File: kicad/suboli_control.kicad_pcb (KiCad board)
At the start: 2 copper layers, 125 x 95 mm, 45 parts, among them J1 DC barrel jack panel header 5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, J2 3.5 mm TRS input panel header, J4 3.5 mm TRS headphone panel he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, J5 MA12070 module power, J6 MA12070 module audio in, SW1 DPST power switch panel header, U1 TLE2426ILP

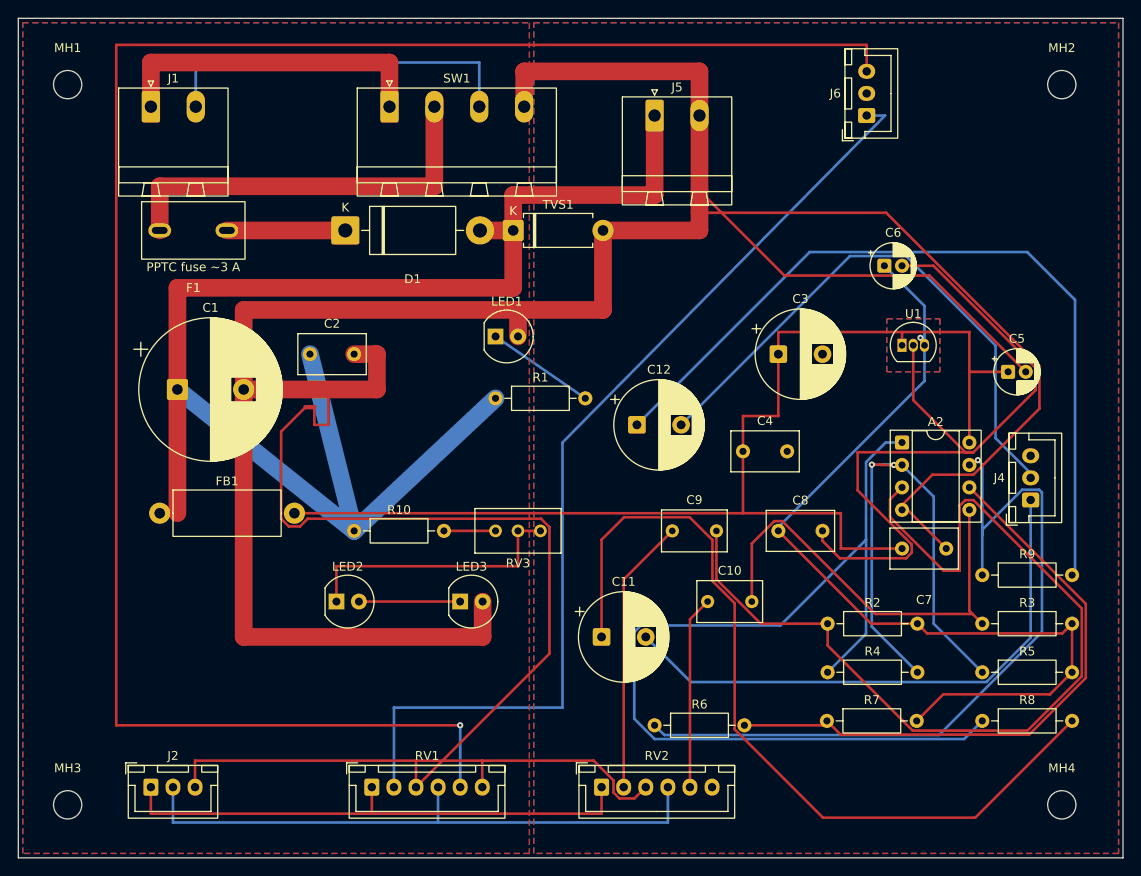
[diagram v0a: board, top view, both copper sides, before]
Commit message: R14: ground stitching vias
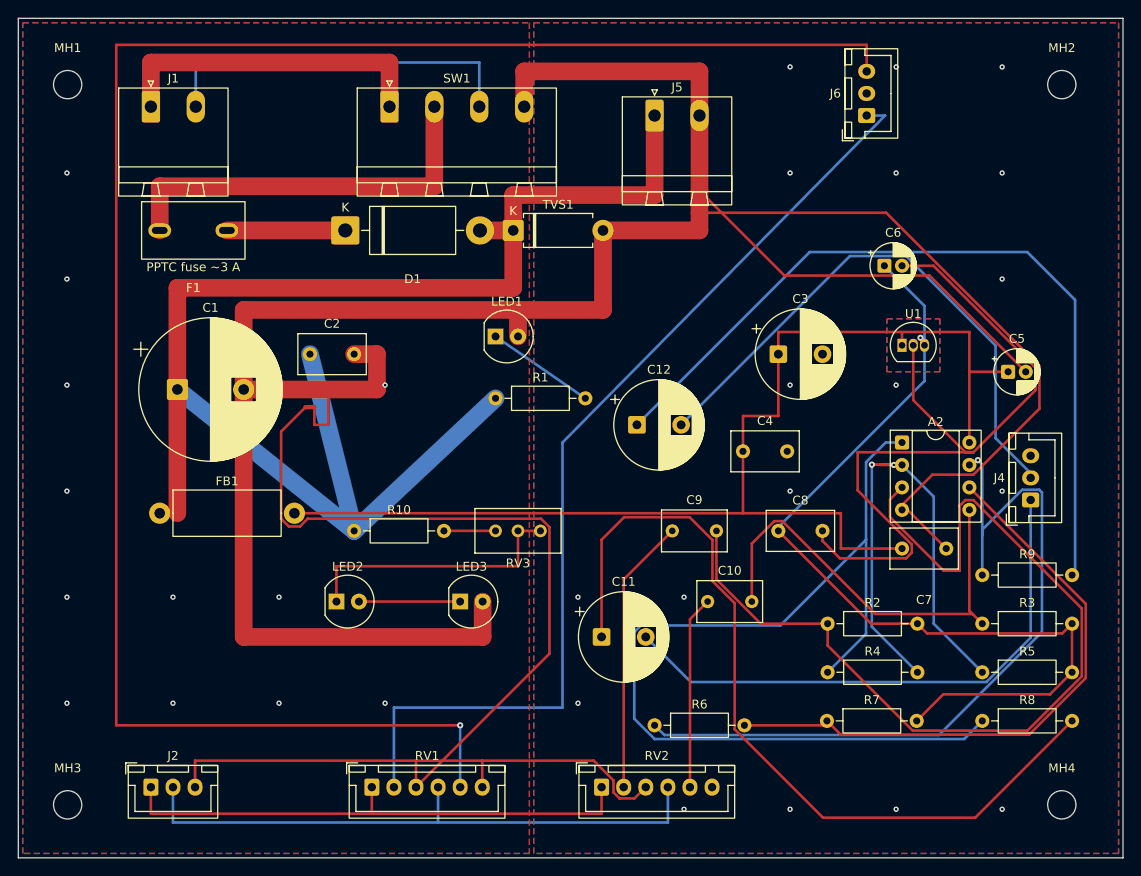
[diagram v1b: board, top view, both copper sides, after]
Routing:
- net /GND_STAR: vias 0 -> 13
- net /GND_SIG: vias 0 -> 18
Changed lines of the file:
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@@
 		(capping no)
 		(filling no)
-		(zone_defaults)
 		(aux_axis_origin 11.92 107)
 		(pcbplotparams
@@
 		(net "/GND_STAR")
 	)
+	(via
+		(at 29.42 77.5)
+		(size 0.6)
+		(drill 0.3)
+		(layers "F.Cu" "B.Cu")
+		(net "/GND_STAR")
+	)
+	(via
+		(at 41.42 53.5)
+		(size 0.6)
+		(drill 0.3)
+		(layers "F.Cu" "B.Cu")
+		(net "/GND_STAR")
+	)
+	(via
+		(at 17.42 65.5)
+		(size 0.6)
+		(drill 0.3)
+		(layers "F.Cu" "B.Cu")
+		(net "/GND_STAR")
+	)
+	(via
+		(at 41.42 77.5)
+		(size 0.6)
+		(drill 0.3)
+		(layers "F.Cu" "B.Cu")
+		(net "/GND_STAR")
+	)
+	(via
+		(at 41.42 89.5)
+		(size 0.6)
+		(drill 0.3)
+		(layers "F.Cu" "B.Cu")
+		(net "/GND_STAR")
+	)
+	(via
+		(at 17.42 29.5)
+		(size 0.6)
+		(drill 0.3)
+		(layers "F.Cu" "B.Cu")
+		(net "/GND_STAR")
+	)
+	(via
+		(at 17.42 41.5)
+		(size 0.6)
+		(drill 0.3)
+		(layers "F.Cu" "B.Cu")
+		(net "/GND_STAR")
+	)
+	(via
+		(at 17.42 77.5)
+		(size 0.6)
+		(drill 0.3)
+		(layers "F.Cu" "B.Cu")
+		(net "/GND_STAR")
+	)
+	(via
+		(at 17.42 53.5)
+		(size 0.6)
+		(drill 0.3)
+		(layers "F.Cu" "B.Cu")
+		(net "/GND_STAR")
+	)
+	(via
+		(at 53.42 89.5)
+		(size 0.6)
+		(drill 0.3)
+		(layers "F.Cu" "B.Cu")
+		(net "/GND_STAR")
+	)
+	(via
+		(at 29.42 89.5)
+		(size 0.6)
+		(drill 0.3)
+		(layers "F.Cu" "B.Cu")
+		(net "/GND_STAR")
+	)
+	(via
+		(at 53.42 53.5)
+		(size 0.6)
+		(drill 0.3)
+		(layers "F.Cu" "B.Cu")
+		(net "/GND_STAR")
+	)
+	(via
+		(at 17.42 89.5)
+		(size 0.6)
+		(drill 0.3)
+		(layers "F.Cu" "B.Cu")
+		(net "/GND_STAR")
+	)
 	(segment
 		(start 94.92 71.441536)
@@
 		(net "/GND_SIG")
 	)
+	(via
+		(at 87.25 101.5)
+		(size 0.6)
+		(drill 0.3)
+		(layers "F.Cu" "B.Cu")
+		(net "/GND_SIG")
+	)
+	(via
+		(at 111.25 17.5)
+		(size 0.6)
+		(drill 0.3)
+		(layers "F.Cu" "B.Cu")
+		(net "/GND_SIG")
+	)
+	(via
+		(at 123.25 65.5)
+		(size 0.6)
+		(drill 0.3)
+		(layers "F.Cu" "B.Cu")
+		(net "/GND_SIG")
+	)
+	(via
+		(at 123.25 101.5)
+		(size 0.6)
+		(drill 0.3)
+		(layers "F.Cu" "B.Cu")
+		(net "/GND_SIG")
+	)
+	(via
+		(at 99.25 101.5)
+		(size 0.6)
+		(drill 0.3)
+		(layers "F.Cu" "B.Cu")
+		(net "/GND_SIG")
+	)
+	(via
+		(at 99.25 53.5)
+		(size 0.6)
+		(drill 0.3)
+		(layers "F.Cu" "B.Cu")
+		(net "/GND_SIG")
+	)
+	(via
+		(at 99.25 17.5)
+		(size 0.6)
+		(drill 0.3)
+		(layers "F.Cu" "B.Cu")
+		(net "/GND_SIG")
+	)
+	(via
+		(at 111.25 53.5)
+		(size 0.6)
+		(drill 0.3)
+		(layers "F.Cu" "B.Cu")
+		(net "/GND_SIG")
+	)
+	(via
+		(at 75.25 77.5)
+		(size 0.6)
+		(drill 0.3)
+		(layers "F.Cu" "B.Cu")
+		(net "/GND_SIG")
+	)
+	(via
+		(at 111.25 101.5)
+		(size 0.6)
+		(drill 0.3)
+		(layers "F.Cu" "B.Cu")
+		(net "/GND_SIG")
+	)
+	(via
+		(at 111.25 29.5)
+		(size 0.6)
+		(drill 0.3)
+		(layers "F.Cu" "B.Cu")
+		(net "/GND_SIG")
+	)
+	(via
+		(at 87.25 77.5)
+		(size 0.6)
+		(drill 0.3)
+		(layers "F.Cu" "B.Cu")
+		(net "/GND_SIG")
+	)
+	(via
+		(at 75.25 89.5)
+		(size 0.6)
+		(drill 0.3)
+		(layers "F.Cu" "B.Cu")
+		(net "/GND_SIG")
+	)
+	(via
+		(at 123.25 29.5)
+		(size 0.6)
+		(drill 0.3)
+		(layers "F.Cu" "B.Cu")
+		(net "/GND_SIG")
+	)
+	(via
+		(at 123.25 41.5)
+		(size 0.6)
+		(drill 0.3)
+		(layers "F.Cu" "B.Cu")
+		(net "/GND_SIG")
+	)
+	(via
+		(at 123.25 17.5)
+		(size 0.6)
+		(drill 0.3)
+		(layers "F.Cu" "B.Cu")
+		(net "/GND_SIG")
+	)
+	(via
+		(at 99.25 29.5)
+		(size 0.6)
+		(drill 0.3)
+		(layers "F.Cu" "B.Cu")
+		(net "/GND_SIG")
+	)
+	(via
+		(at 99.25 65.5)
+		(size 0.6)
+		(drill 0.3)
+		(layers "F.Cu" "B.Cu")
+		(net "/GND_SIG")
+	)

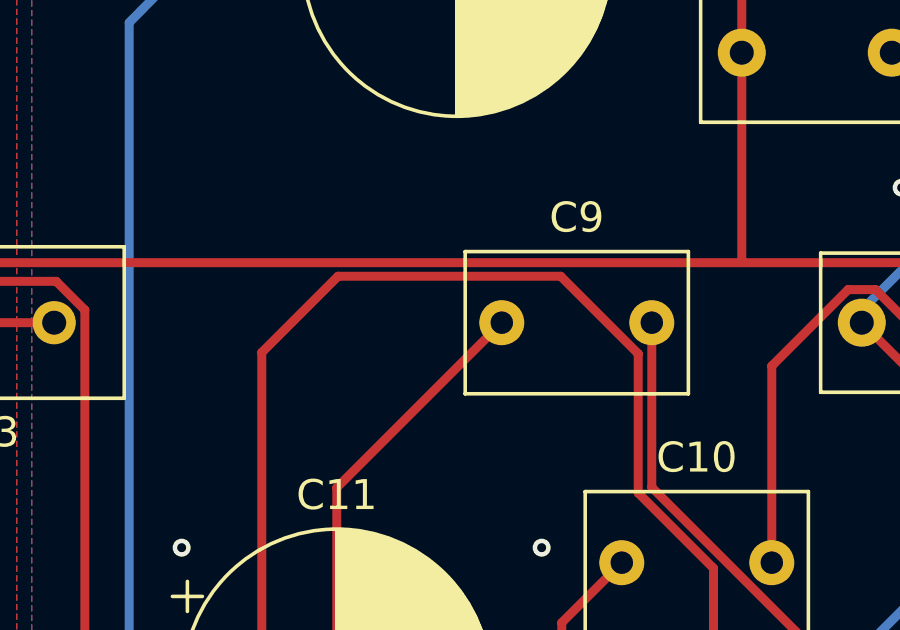
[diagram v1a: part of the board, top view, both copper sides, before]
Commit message: R15: Flag 3 clearance fix - HP_L_SER spacing, board final 0/0
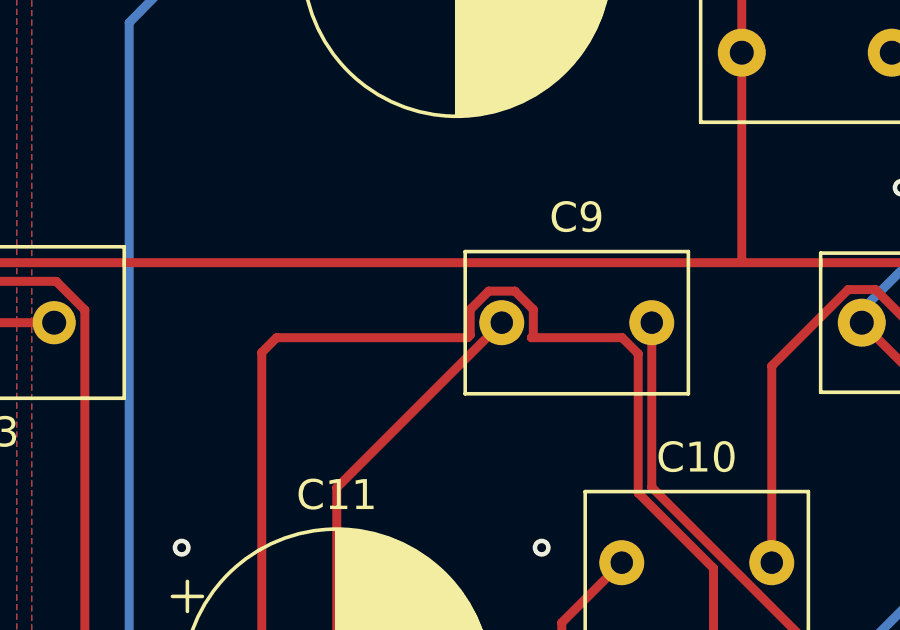
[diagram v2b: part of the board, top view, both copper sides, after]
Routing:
- net /HP_L_SER: track 95.0 -> 95.7 mm
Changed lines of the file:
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@@
 	)
 	(segment
-		(start 87.884247 68.452)
-		(end 80.463449 68.452)
+		(start 92.978 92.456464)
+		(end 92.978 78.184977)
+		(width 0.3)
+		(layer "F.Cu")
+		(net "/HP_L_SER")
+	)
+	(segment
+		(start 86.355753 68.948)
+		(end 85.484247 68.948)
+		(width 0.3)
+		(layer "F.Cu")
+		(net "/HP_L_SER")
+	)
+	(segment
+		(start 89.932247 70.5)
+		(end 86.907753 70.5)
+		(width 0.3)
+		(layer "F.Cu")
+		(net "/HP_L_SER")
+	)
+	(segment
+		(start 78.415449 70.5)
+		(end 77.92 70.995449)
+		(width 0.3)
+		(layer "F.Cu")
+		(net "/HP_L_SER")
+	)
+	(segment
+		(start 86.972 69.564247)
+		(end 86.355753 68.948)
+		(width 0.3)
+		(layer "F.Cu")
+		(net "/HP_L_SER")
+	)
+	(segment
+		(start 85.484247 68.948)
+		(end 84.868 69.564247)
+		(width 0.3)
+		(layer "F.Cu")
+		(net "/HP_L_SER")
+	)
+	(segment
+		(start 86.972 70.435753)
+		(end 86.972 69.564247)
+		(width 0.3)
+		(layer "F.Cu")
+		(net "/HP_L_SER")
+	)
+	(segment
+		(start 86.907753 70.5)
+		(end 86.972 70.435753)
+		(width 0.3)
+		(layer "F.Cu")
+		(net "/HP_L_SER")
+	)
+	(segment
+		(start 84.868 69.564247)
+		(end 84.868 70.412776)
+		(width 0.3)
+		(layer "F.Cu")
+		(net "/HP_L_SER")
+	)
+	(segment
+		(start 90.468 71.035753)
+		(end 89.932247 70.5)
 		(width 0.3)
 		(layer "F.Cu")
@@
 	)
 	(segment
-		(start 80.463449 68.452)
-		(end 77.92 70.995449)
+		(start 92.978 78.184977)
+		(end 90.468 75.674977)
+		(width 0.3)
+		(layer "F.Cu")
+		(net "/HP_L_SER")
+	)
+	(segment
+		(start 77.92 70.995449)
+		(end 77.92 82)
 		(width 0.3)
 		(layer "F.Cu")
@@
 	)
 	(segment
+		(start 84.780776 70.5)
+		(end 78.415449 70.5)
+		(width 0.3)
+		(layer "F.Cu")
+		(net "/HP_L_SER")
+	)
+	(segment
 		(start 90.468 75.674977)
 		(end 90.468 71.035753)
@@
 	)
 	(segment
-		(start 90.468 71.035753)
-		(end 87.884247 68.452)
-		(width 0.3)
-		(layer "F.Cu")
-		(net "/HP_L_SER")
-	)
-	(segment
-		(start 92.978 78.184977)
-		(end 90.468 75.674977)
-		(width 0.3)
-		(layer "F.Cu")
-		(net "/HP_L_SER")
-	)
-	(segment
-		(start 92.978 92.456464)
-		(end 92.978 78.184977)
+		(start 84.868 70.412776)
+		(end 84.780776 70.5)
 		(width 0.3)
 		(layer "F.Cu")
@@
 		(width 0.3)
 		(layer "F.Cu")
-		(net "/HP_L_SER")
-	)
-	(segment
-		(start 77.92 70.995449)
-		(end 77.92 82)
-		(width 0.3)
-		(layer "F.Cu")
